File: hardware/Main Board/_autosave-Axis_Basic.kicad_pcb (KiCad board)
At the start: 4 copper layers, 42 x 42 mm, 49 parts, among them J1 USB_C_Receptacle_USB2.0, J2 JST_PH, J3 JST_PH, J4 S2B-PH-K-S, J5 1175-1628-ND, J6 1-84952-4, SW1 RKB2SJK, SW2 RKB2SJK, U1 TLV493D, U2 UA78M33CDCYR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

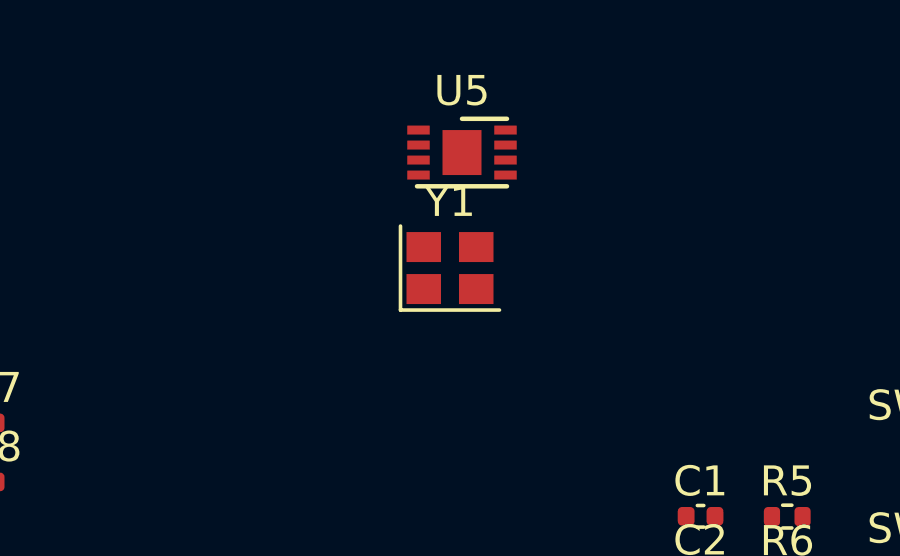
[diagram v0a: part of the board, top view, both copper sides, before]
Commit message: Add 32Mhz crystal
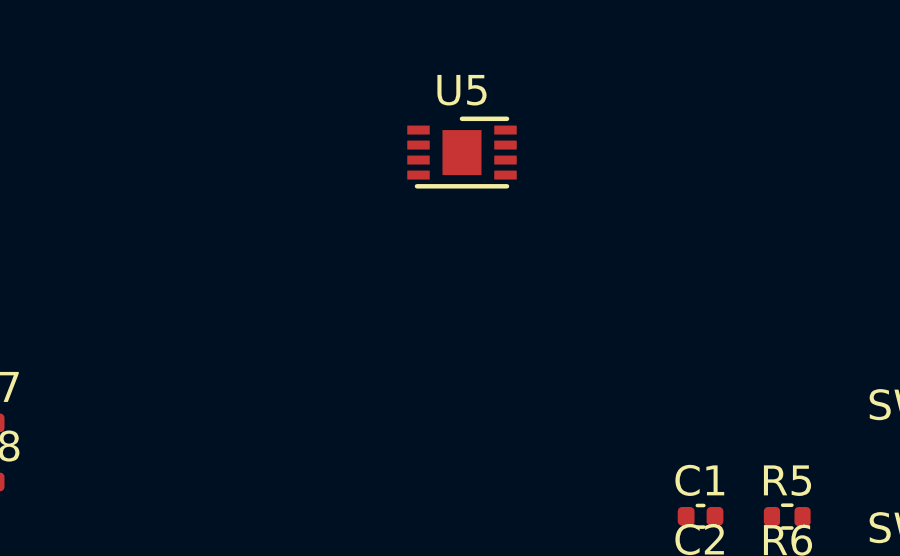
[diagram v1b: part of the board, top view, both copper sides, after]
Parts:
- removed Y1: SG-210STF 48.0000ML0, Crystal:Crystal_SMD_2520-4Pin_2.5x2.0mm
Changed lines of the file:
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@@
-    )
-  )
-  (footprint "Crystal:Crystal_SMD_2520-4Pin_2.5x2.0mm" (layer "F.Cu")
-    (at 191.5525 68.91)
-    (descr "SMD Crystal SERIES SMD2520/4 http://www.newxtal.com/UploadFiles/Images/2012-11-12-09-29-09-776.pdf, 2.5x2.0mm^2 package")
-    (tags "SMD SMT crystal")
-    (property "Sheetfile" "Axis_Basic.kicad_sch")
-    (property "Sheetname" "")
-    (property "ki_description" "Two pin crystal")
-    (property "ki_keywords" "quartz ceramic resonator oscillator")
-    (attr smd)
-    (fp_text reference "Y1" (at 0 -2.2) (layer "F.SilkS")
-        (effects (font (size 1 1) (thickness 0.15)))
-    )
-    (fp_text value "SG-210STF 48.0000ML0" (at 0 2.2) (layer "F.Fab")
-        (effects (font (size 1 1) (thickness 0.15)))
-    )
-    (fp_text user "${REFERENCE}" (at 0 0) (layer "F.Fab")
-        (effects (font (size 0.6 0.6) (thickness 0.09)))
-    )
-    (fp_line (start -1.65 -1.4) (end -1.65 1.4)
-      (stroke (width 0.12) (type solid)) (layer "F.SilkS"))
-    (fp_line (start -1.65 1.4) (end 1.65 1.4)
-      (stroke (width 0.12) (type solid)) (layer "F.SilkS"))
-    (fp_line (start -1.7 -1.5) (end -1.7 1.5)
-      (stroke (width 0.05) (type solid)) (layer "F.CrtYd"))
-    (fp_line (start -1.7 1.5) (end 1.7 1.5)
-      (stroke (width 0.05) (type solid)) (layer "F.CrtYd"))
-    (fp_line (start 1.7 -1.5) (end -1.7 -1.5)
-      (stroke (width 0.05) (type solid)) (layer "F.CrtYd"))
-    (fp_line (start 1.7 1.5) (end 1.7 -1.5)
-      (stroke (width 0.05) (type solid)) (layer "F.CrtYd"))
-    (fp_line (start -1.25 -0.9) (end -1.15 -1)
-      (stroke (width 0.1) (type solid)) (layer "F.Fab"))
-    (fp_line (start -1.25 0) (end -0.25 1)
-      (stroke (width 0.1) (type solid)) (layer "F.Fab"))
-    (fp_line (start -1.25 0.9) (end -1.25 -0.9)
-      (stroke (width 0.1) (type solid)) (layer "F.Fab"))
-    (fp_line (start -1.15 -1) (end 1.15 -1)
-      (stroke (width 0.1) (type solid)) (layer "F.Fab"))
-    (fp_line (start -1.15 1) (end -1.25 0.9)
-      (stroke (width 0.1) (type solid)) (layer "F.Fab"))
-    (fp_line (start 1.15 -1) (end 1.25 -0.9)
-      (stroke (width 0.1) (type solid)) (layer "F.Fab"))
-    (fp_line (start 1.15 1) (end -1.15 1)
-      (stroke (width 0.1) (type solid)) (layer "F.Fab"))
-    (fp_line (start 1.25 -0.9) (end 1.25 0.9)
-      (stroke (width 0.1) (type solid)) (layer "F.Fab"))
-    (fp_line (start 1.25 0.9) (end 1.15 1)
-      (stroke (width 0.1) (type solid)) (layer "F.Fab"))
-    (pad "1" smd rect (at -0.875 0.7) (size 1.15 1) (layers "F.Cu" "F.Paste" "F.Mask")
-      (net 14 "Net-(C18-Pad2)") (pinfunction "1") (pintype "passive"))
-    (pad "2" smd rect (at 0.875 0.7) (size 1.15 1) (layers "F.Cu" "F.Paste" "F.Mask")
-      (net 13 "Net-(C17-Pad2)") (pinfunction "2") (pintype "passive"))
-    (pad "3" smd rect (at 0.875 -0.7) (size 1.15 1) (layers "F.Cu" "F.Paste" "F.Mask"))
-    (pad "4" smd rect (at -0.875 -0.7) (size 1.15 1) (layers "F.Cu" "F.Paste" "F.Mask"))
-    (model "${KICAD6_3DMODEL_DIR}/Crystal.3dshapes/Crystal_SMD_2520-4Pin_2.5x2.0mm.wrl"
-      (offset (xyz 0 0 0))
-      (scale (xyz 1 1 1))
-      (rotate (xyz 0 0 0))
     )
   )
